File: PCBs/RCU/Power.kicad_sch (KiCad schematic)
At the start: 30 parts, among them J100 Conn_01x02, U100 AP63203WU, U102 AZ1117-3.3, U103 AP63203WU

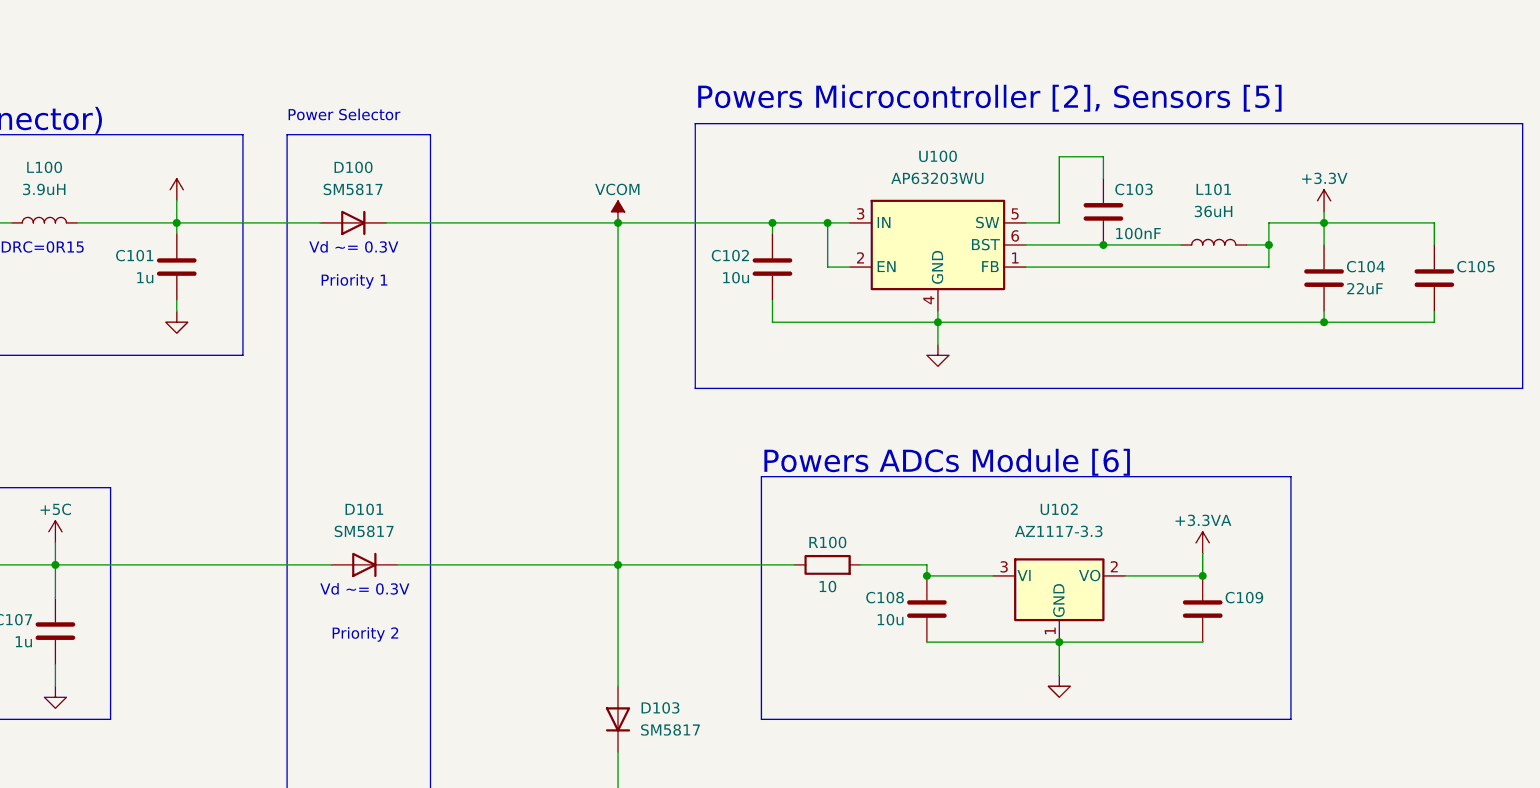
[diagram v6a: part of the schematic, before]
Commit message: Corrected C302 and C305 values in motor drive units, should be 22nF, not 22uF
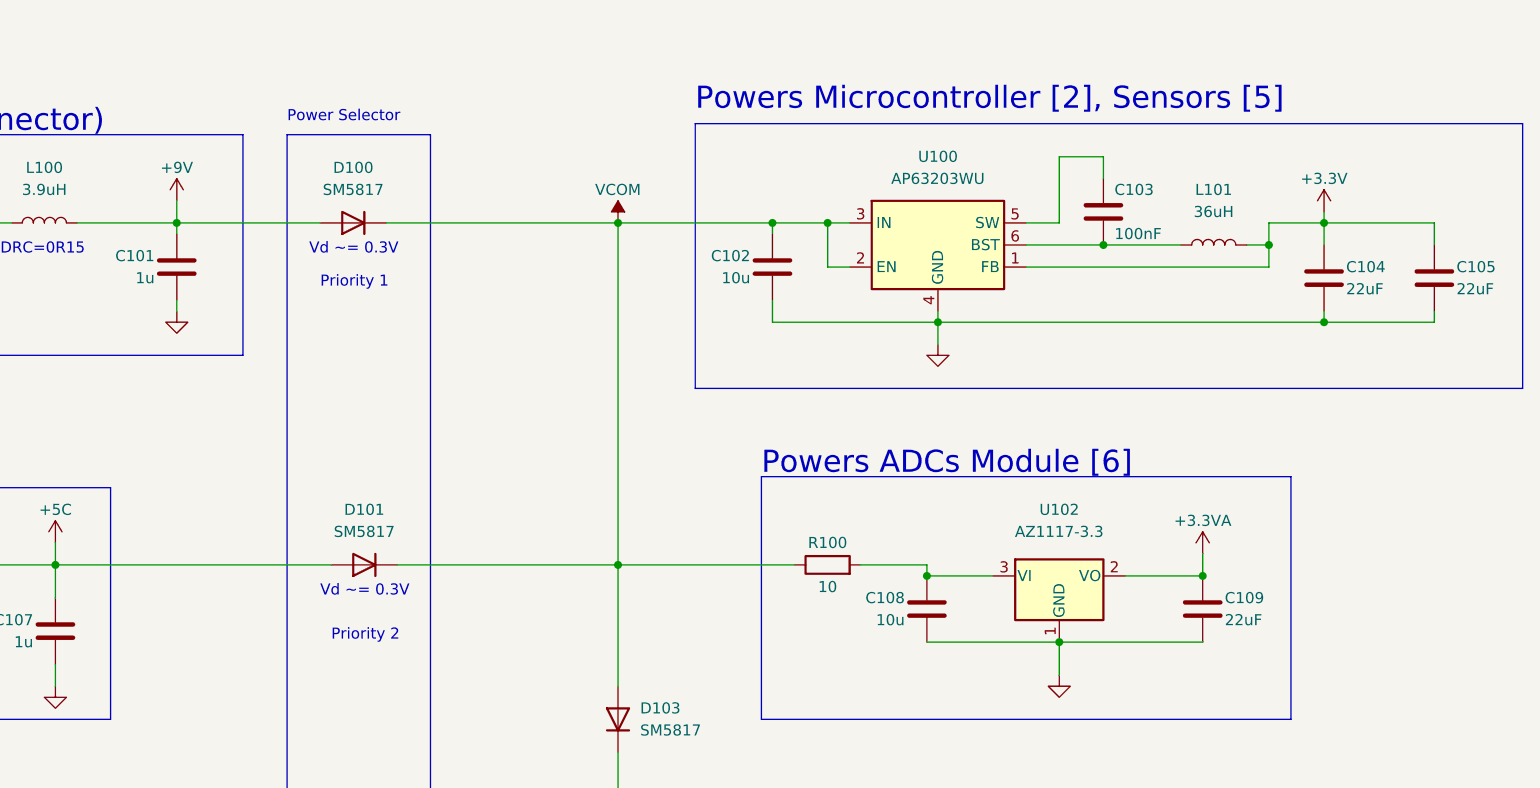
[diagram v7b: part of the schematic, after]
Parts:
- C105, C109: value (none) -> 22uF
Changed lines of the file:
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@@
       (effects (font (size 1.27 1.27)) hide)
     )
-    (property "Value" "" (id 1) (at 93.98 49.53 0))
+    (property "Value" "+9V" (id 1) (at 93.98 49.53 0))
     (property "Footprint" "" (id 2) (at 93.98 53.34 0)
       (effects (font (size 1.27 1.27)) hide)
@@
       (effects (font (size 1.27 1.27)) (justify left))
     )
-    (property "Value" "" (id 1) (at 214.63 101.6 0)
+    (property "Value" "22uF" (id 1) (at 214.63 101.6 0)
       (effects (font (size 1.27 1.27)) (justify left))
     )
@@
       (effects (font (size 1.27 1.27)) (justify left))
     )
-    (property "Value" "" (id 1) (at 241.3 63.5 0)
+    (property "Value" "22uF" (id 1) (at 241.3 63.5 0)
       (effects (font (size 1.27 1.27)) (justify left))
     )

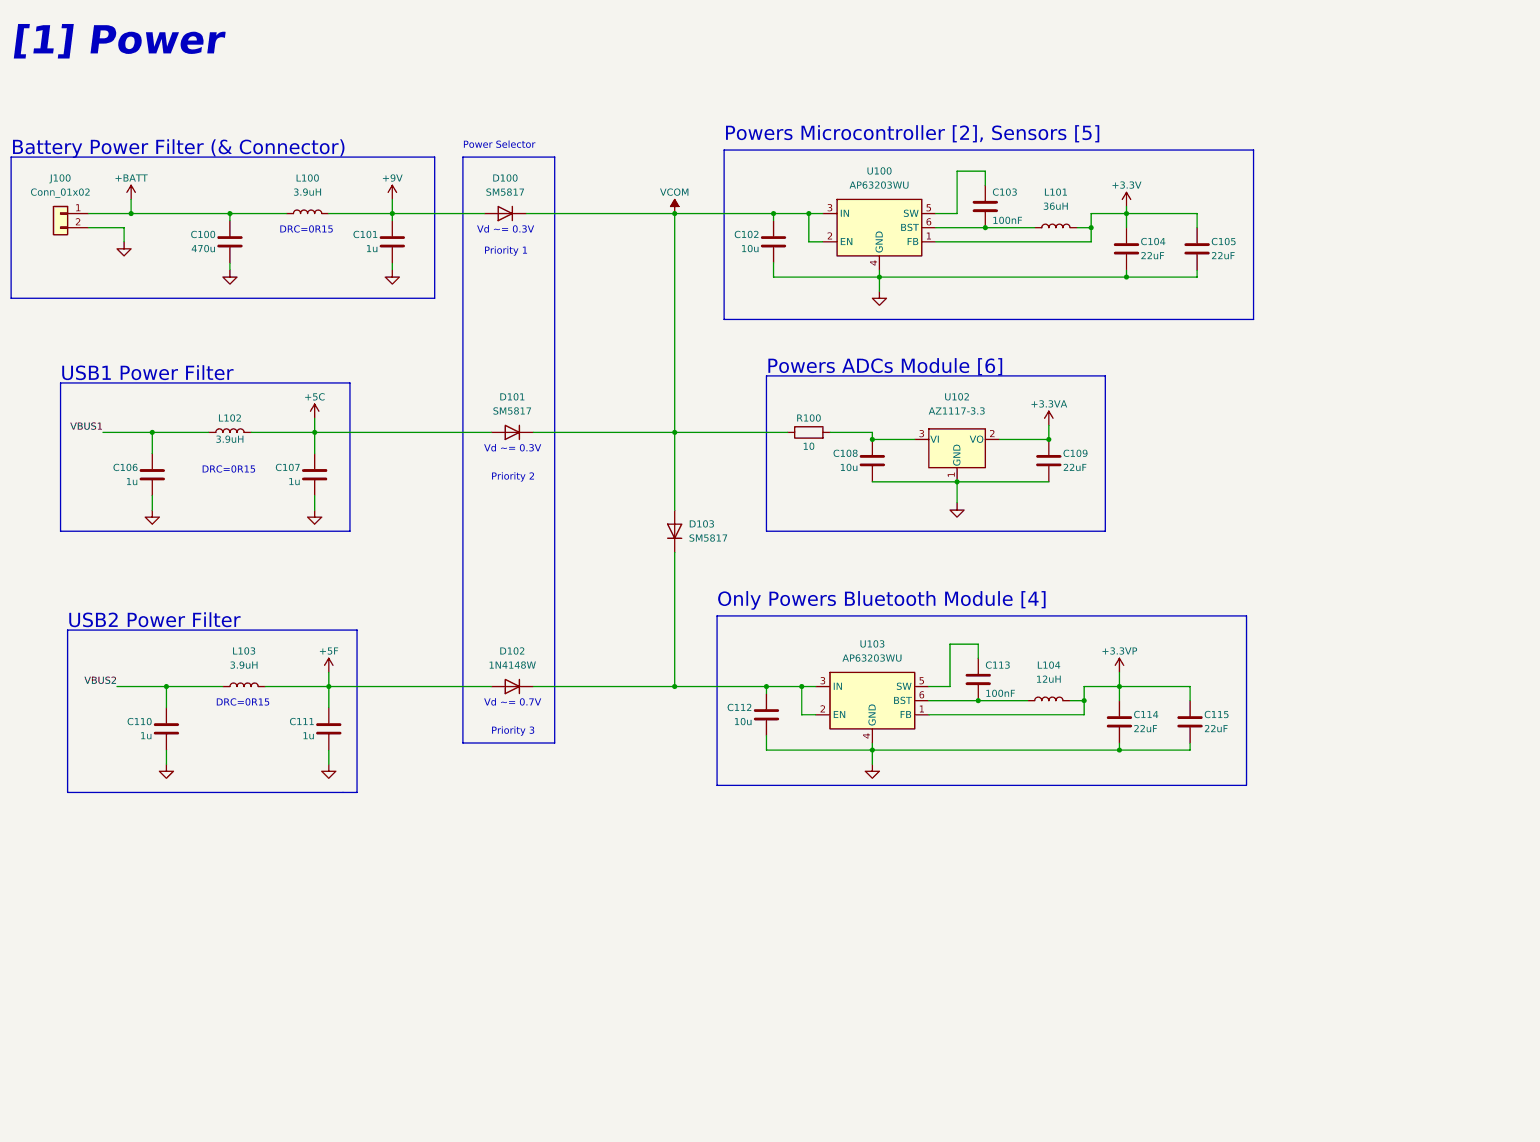
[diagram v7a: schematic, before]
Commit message: Added 6V adjustable regulator to power motors and encoders
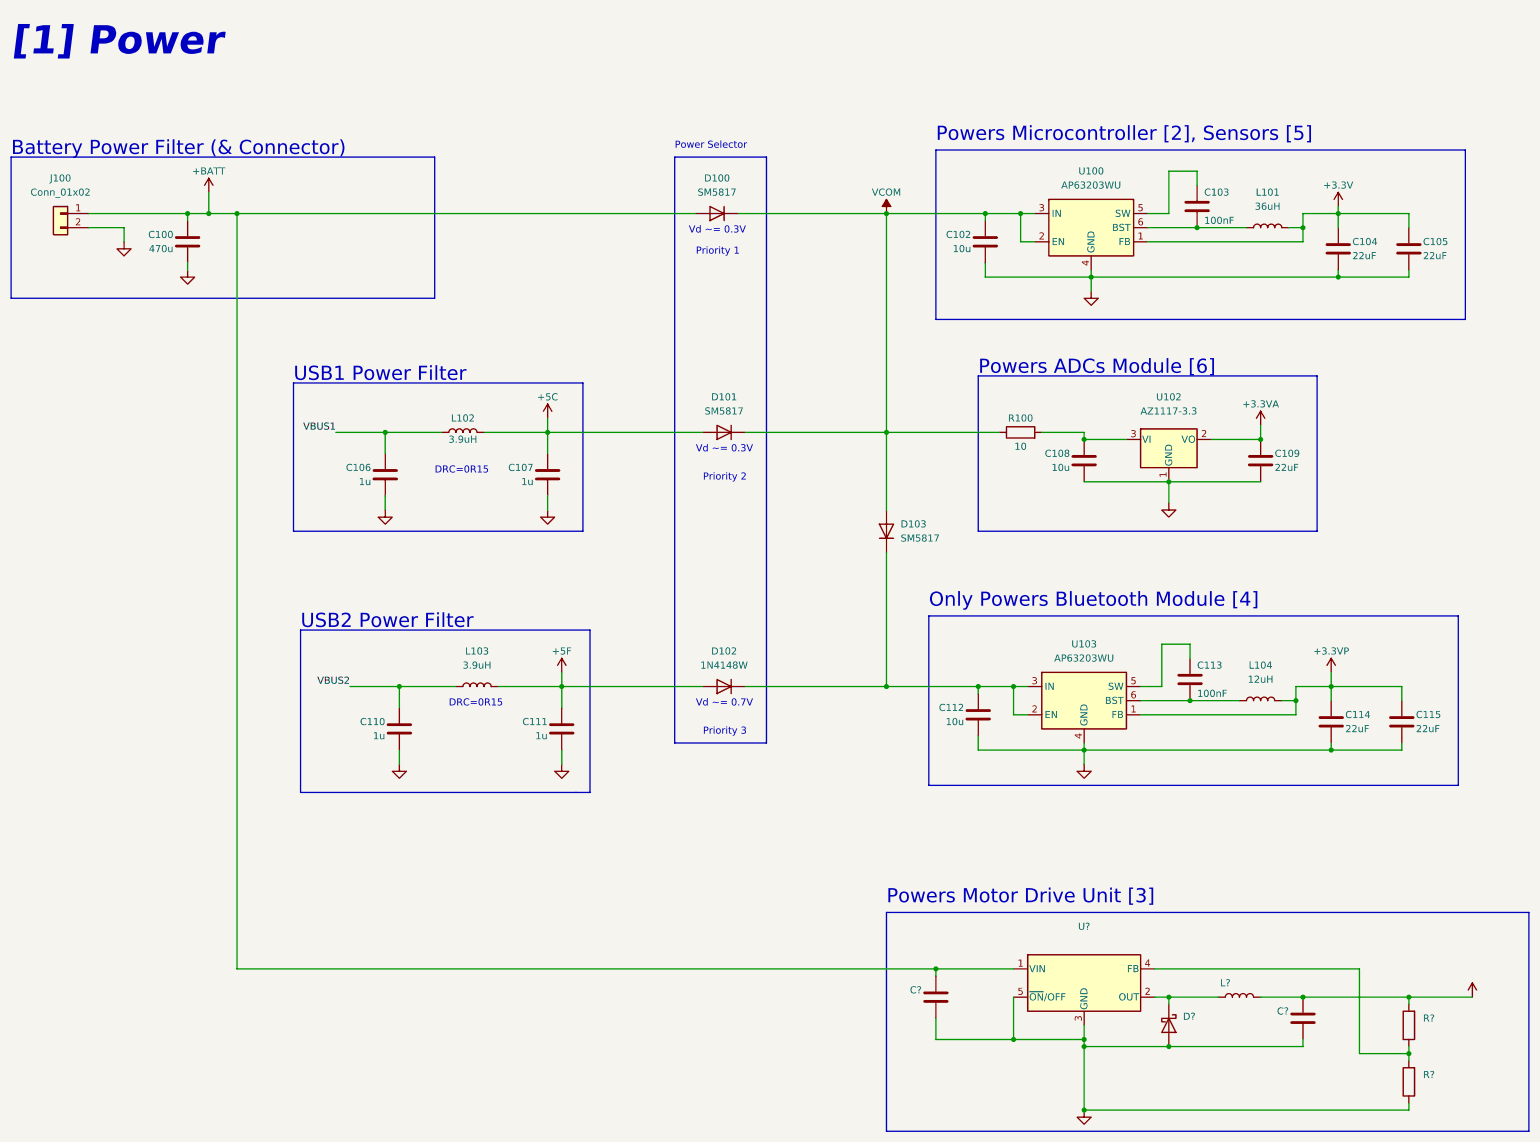
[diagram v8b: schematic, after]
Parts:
- removed C101: 1u, symbol Device:C
- removed L100: 3.9uH, symbol Device:L
- added C? (x2): (no value), symbol Device:C
- added D?: (no value), symbol Diode:1N5822
- added L?: (no value), symbol Device:L
- added R? (x2): (no value), symbol Device:R
- added U?: (no value), symbol Regulator_Switching:LM2576S-ADJ
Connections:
- net +9V is gone; now on net +BATT: D100.2 (A)
- net +BATT: now also C?.1, U?.1 (VIN)
- net GND: now also C?.2, C?.2, D?.2 (A), R?.1, U?.3 (GND), U?.5 (~{ON}/OFF)
- new net: D?.1 (K), L?.1, U?.2 (OUT)
- new net: R?.1, R?.2, U?.4 (FB)
- new net +6V: C?.1, L?.2, R?.2
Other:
- note added: "Powers Motor Drive Unit [3]"
- moved on the sheet: C100, C102, C103, C104, C105, C106, C107, C108, C109, C110, C111, C112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
